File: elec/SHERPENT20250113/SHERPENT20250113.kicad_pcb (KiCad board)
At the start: 4 copper layers, 130.2 x 68.2 mm, 125 parts, among them J1 2137160001, J2 Conn_01x03_Socket, J3 Conn_01x03_Socket, Q1 NMOS, Q2 PMOS, Q3 NMOS, Q4 PMOS, SW1 CT1102, SW2 SW_Push, U1 MCP73831T-2ACI_OT, U2 TPS61288LRQQR, U4 TP4056, U5 LD1117S33TR_SOT223, U6 AN034_ANTENNA, U7 ESP32-C3, Y1 40MHz

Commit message: DRC ok
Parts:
- moved TP4 0.68 mm to (174.2, 86.2)
- moved R20 0.20 mm to (185.8, 83.2)
- moved R17 0.20 mm to (185.8, 79.8)
- moved R16 0.20 mm to (185.8, 81.5)
- moved C26 0.16 mm to (192.9, 77.0)
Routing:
- net GND: track 138.0 -> 139.8 mm
- net /VBATT: track 118.6 -> 117.8 mm
- net /VUSB: track 128.2 -> 129.0 mm
- net /StayOn: track 67.5 -> 68.2 mm
- net /Moteur2_PWM: track 62.6 -> 63.2 mm

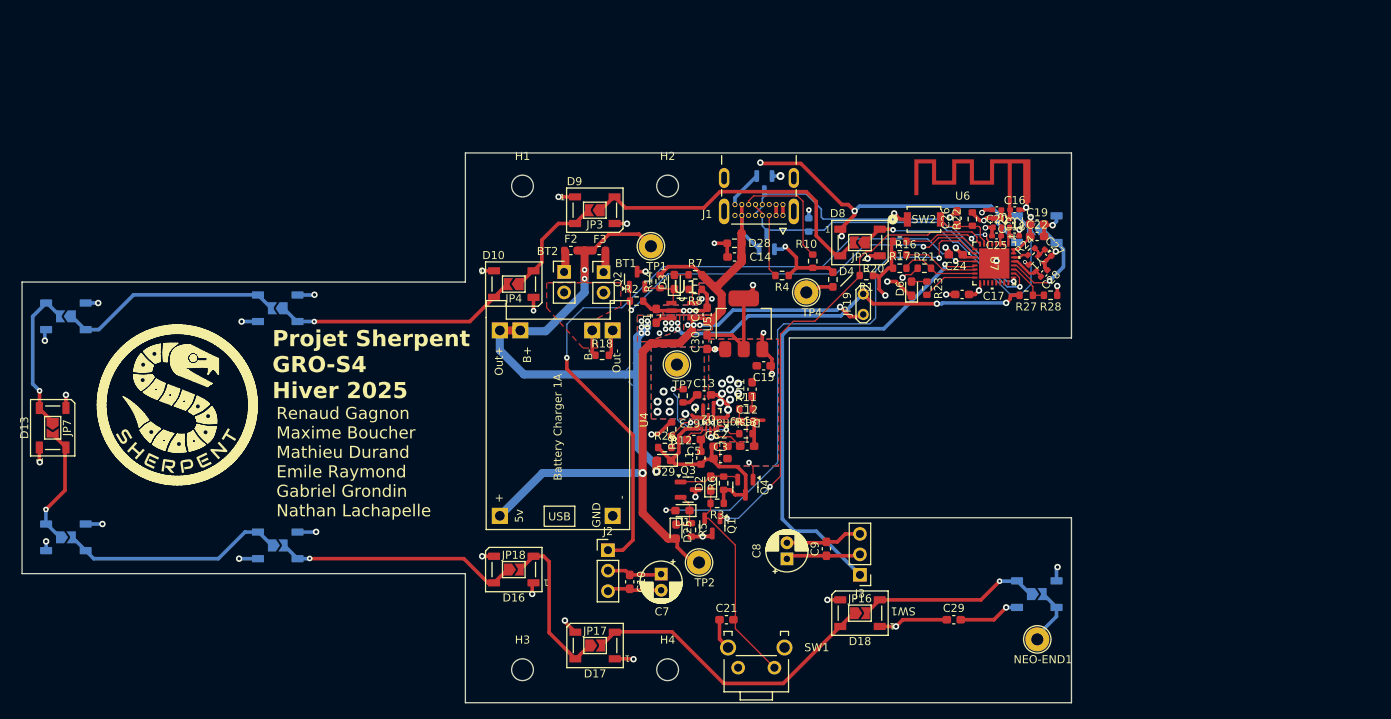
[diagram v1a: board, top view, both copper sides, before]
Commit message: Silkscreen done
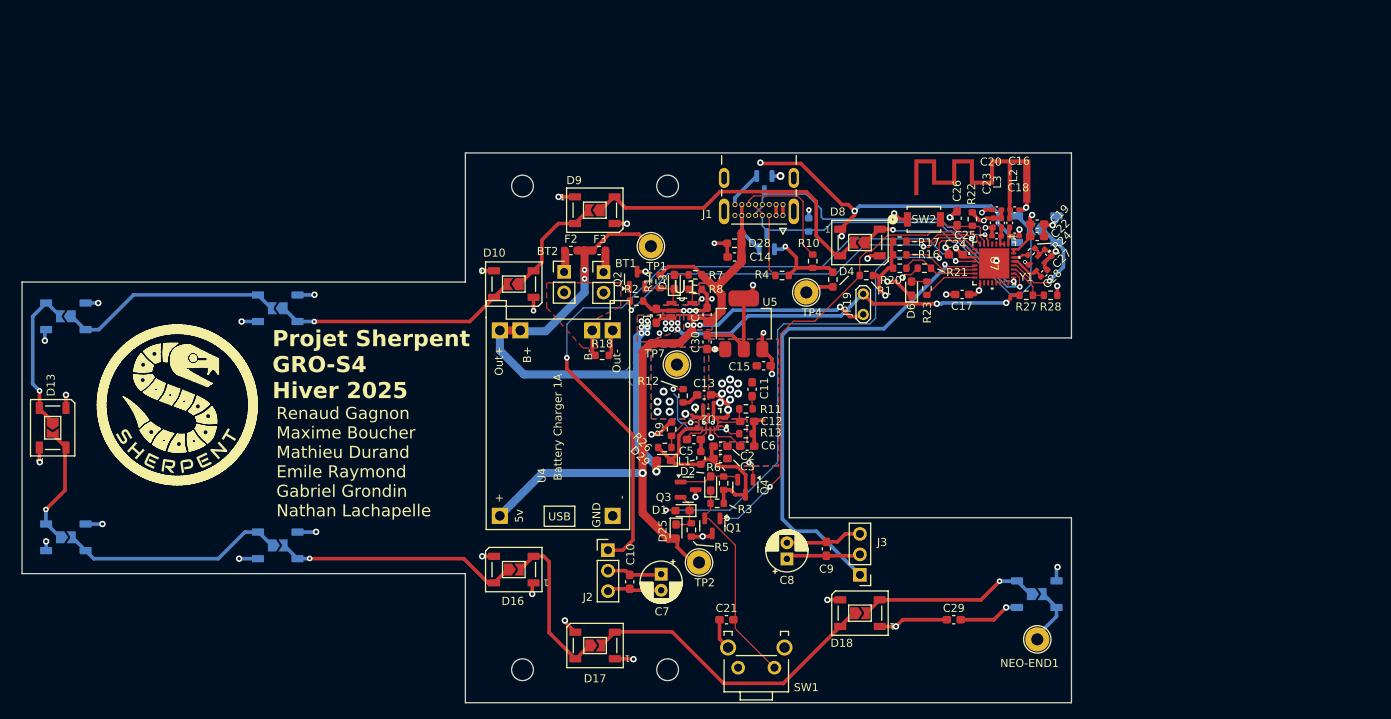
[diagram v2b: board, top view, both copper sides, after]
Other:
- board text removed: "J3"
- board text removed: "SW1"

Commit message: Conn neopx
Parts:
- removed D13, D14, D15: WS2812B, LED_SMD:LED_WS2812B_PLCC4_5.0x5.0mm_P3.2mm
- removed JP7, JP8, JP9: SolderJumper_2_Open, Jumper:SolderJumper-2_P1.3mm_Open_TrianglePad1.0x1.5mm
- added J4: Conn_01x03_Socket, Connector_PinHeader_2.54mm:PinHeader_1x03_P2.54mm_Vertical, F.Cu at (194.9, 133.2)
- moved JP6 65.6 mm to (137.9, 124.0), turned to 0 degrees
- moved D12 65.5 mm to (137.9, 123.9), turned to 180 degrees
- moved D11 30.1 mm to (138.1, 81.8)
- moved JP5 30.1 mm to (138.0, 81.8)
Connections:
- net Net-(D19-DOUT) renamed /neo_end
- D12 pad 2: Net-(D12-DOUT) -> /NEO_Row2
- JP6 pad 2: Net-(D12-DOUT) -> /NEO_Row2
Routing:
- net Net-(D14-DOUT): track 28.0 -> 0.00 mm
- net Net-(D11-DOUT): track 28.0 -> 48.8 mm
- net Net-(D10-DOUT): track 30.4 -> 9.92 mm
- net Net-(D12-DOUT): track 18.7 -> 0.00 mm, vias 1 -> 0
- net /NEO_Row2: track 30.5 -> 12.7 mm
- net Net-(D13-DOUT): track 15.3 -> 0.00 mm, vias 1 -> 0
- net +9V: track 111.0 -> 102.8 mm, vias 23 -> 18
- net /neo_end: track 7.36 -> 14.6 mm
- net GND: track 139.8 -> 133.8 mm, vias 48 -> 45
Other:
- board size 130.2 x 68.2 mm -> 75.2 x 68.2 mm
- board text added: "+ D G"
- board text added: "neopx"

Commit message: Gerber générés et PCB envoyé pour la fabrication
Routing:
- net +9V: track 102.8 -> 104.4 mm
- net Net-(U2-FB): track 14.0 -> 14.6 mm

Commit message: pcb V2 commencé
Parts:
- removed C1, C4: 4.7u, Capacitor_SMD:C_0603_1608Metric_Pad1.08x0.95mm_HandSolder
- removed C14, C24: 100n, Capacitor_SMD:C_0603_1608Metric_Pad1.08x0.95mm_HandSolder
- removed C18: 1.8p, Capacitor_SMD:C_0402_1005Metric_Pad0.74x0.62mm_HandSolder
- removed C19: 10n, Capacitor_SMD:C_0603_1608Metric_Pad1.08x0.95mm_HandSolder
- removed C20: 10u, Capacitor_SMD:C_0402_1005Metric_Pad0.74x0.62mm_HandSolder
- removed C22: 1u, Capacitor_SMD:C_0603_1608Metric_Pad1.08x0.95mm_HandSolder
- removed C23: 100n, Capacitor_SMD:C_0402_1005Metric_Pad0.74x0.62mm_HandSolder
- removed C25: 1u, Capacitor_SMD:C_0402_1005Metric_Pad0.74x0.62mm_HandSolder
- removed C27, C28: 15p, Capacitor_SMD:C_0402_1005Metric_Pad0.74x0.62mm_HandSolder
- removed D25: D_Schottky, LED_SMD:LED_0603_1608Metric_Pad1.05x0.95mm_HandSolder
- removed D29: D, Diode_SMD:D_0603_1608Metric_Pad1.05x0.95mm_HandSolder
- removed D3: LED, LED_SMD:LED_0603_1608Metric_Pad1.05x0.95mm_HandSolder
- removed D4: D_Zener, Resistor_SMD:R_0603_1608Metric_Pad0.98x0.95mm_HandSolder
- removed JP19: Jumper_2_Bridged, TestPoint:TestPoint_2Pads_Pitch2.54mm_Drill0.8mm
- removed L2: 2.7n, Inductor_SMD:L_0402_1005Metric_Pad0.77x0.64mm_HandSolder
- removed L3: 2n, Inductor_SMD:L_0402_1005Metric_Pad0.77x0.64mm_HandSolder
- removed Q4: PMOS, Package_TO_SOT_SMD:SOT-23
- removed R17, R20, R25: 10k, Resistor_SMD:R_0603_1608Metric
- removed R18, R21, R26: 0, Resistor_SMD:R_0603_1608Metric
- removed R24: 0, Resistor_SMD:R_0402_1005Metric_Pad0.72x0.64mm_HandSolder
- removed TP1: VBATT, TestPoint:TestPoint_Loop_D2.54mm_Drill1.5mm_Beaded
- removed U1: MCP73831T-2ACI_OT, MCP73831T_2ACI_OT:SOT95P280X145-5N
- removed U6: AN034_ANTENNA, AN034_ANTENNA:AN034_ANTENNA
- removed U7: ESP32-C3, ESP32_C3:QFN32_5X5_EXP-L
- removed Y1: 40MHz, 830059627:SMD_059627_WRE-L
- added C31: 47u, Capacitor_SMD:C_0603_1608Metric_Pad1.08x0.95mm_HandSolder, F.Cu at (161.8, 94.8)
- added C32: 47u, Capacitor_SMD:C_0603_1608Metric_Pad1.08x0.95mm_HandSolder, F.Cu at (161.8, 96.2)
- added C33: 47u, Capacitor_SMD:C_0603_1608Metric_Pad1.08x0.95mm_HandSolder, F.Cu at (161.8, 97.8)
- added JP7: BOOT, Connector_PinHeader_2.54mm:PinHeader_1x02_P2.54mm_Vertical, F.Cu at (178.8, 86.0)
- added Q5: PMOS, Package_TO_SOT_SMD:SOT-223, F.Cu at (186.2, 99.5)
- added R15: 10k, Resistor_SMD:R_0603_1608Metric, F.Cu at (242.9, 99.4)
- added R19: 10k, Resistor_SMD:R_0603_1608Metric, F.Cu at (242.9, 101.9)
- added SW3: BOOT, CS1213AGF160:SW_CS1213AG_CRS, F.Cu at (183.5, 86.8)
- added U3: LM66200DRLR, LM66200DRLR:SOT-5X3_DRL_TEX-L, F.Cu at (170.0, 88.2)
- added U8: ESP32-C3-WROOM-02, RF_Module:ESP32-C3-WROOM-02, F.Cu at (196.5, 82.2)
- C16: value 1.8p -> 10u; footprint Capacitor_SMD:C_0402_1005Metric_Pad0.74x0.62mm_HandSolder -> Capacitor_SMD:C_0603_1608Metric_Pad1.08x0.95mm_HandSolder
- C17: value 100n -> 0.1u
- C26: value 10n -> 0.1u
- H1, H2, H3, H4: footprint MountingHole:MountingHole_2.7mm_M2.5 -> MountingHole:MountingHole_3.2mm_M3
- L1: footprint Inductor_SMD:L_0603_1608Metric -> Inductor_SMD:L_1206_3216Metric
- NEO-END1: value TestPoint -> Neo-end
- Q1: value NMOS -> PMOS; footprint Package_TO_SOT_SMD:SOT-23 -> Package_TO_SOT_SMD:SOT-223
- Q2: value PMOS -> Q_NMOS_GSD
- Q3: value NMOS -> Q_NMOS_GSD
- R14, R2: value 100k -> 0; footprint Resistor_SMD:R_0603_1608Metric -> Resistor_SMD:R_1206_3216Metric
- R7: value 470 -> 0
- R8: value 2k -> 0; footprint Resistor_SMD:R_0603_1608Metric -> Resistor_SMD:R_1206_3216Metric
- SW2: value SW_Push -> RESET
- moved Q2 49.0 mm to (196.5, 107.5)
- moved TP2 41.3 mm to (158.5, 78.5)
- moved R2 34.0 mm to (174.5, 113.8)
- moved Q1 23.9 mm to (185.5, 108.5)
- moved R1 22.8 mm to (194.8, 102.8)
- moved R7 20.8 mm to (156.8, 104.5)
- moved C17 20.7 mm to (187.9, 66.5)
- moved R23 20.7 mm to (183.5, 65.8)
- moved R27 20.7 mm to (195.8, 66.6)
- moved R28 20.7 mm to (198.8, 66.6)
- moved R22 20.7 mm to (189.1, 57.2)
- moved C16 20.7 mm to (194.4, 56.0)
- moved C26 20.7 mm to (187.2, 57.1)
- moved D6 20.7 mm to (181.6, 65.8)
- moved TP7 18.8 mm to (177.0, 95.3)
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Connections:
- C15 pad 1: +9V -> /VDIODE
- C16 pad 1: Net-(U6-FP) -> +3.3V
- C2 pad 1: Net-(D29-K) -> Net-(U2-VIN)
- C29 pad 1: +9V -> +3.3V
- C3 pad 1: Net-(D29-K) -> Net-(U2-VIN)
- D10 pad 1: +9V -> +3.3V
- D11 pad 1: +9V -> +3.3V
- D12 pad 1: +9V -> +3.3V
- D16 pad 1: +9V -> +3.3V
- D17 pad 1: +9V -> +3.3V
- D18 pad 1: +9V -> +3.3V
- D19 pad 1: +9V -> +3.3V
- D7 pad 1: +9V -> +3.3V
- D8 pad 1: +9V -> +3.3V
- D9 pad 1: +9V -> +3.3V
- F2 pad 2: /VBATT -> Net-(Q5-S)
- F3 pad 2: /VBATT -> Net-(Q5-S)
- L1 pad 1: Net-(D29-K) -> Net-(U2-VIN)
- Q1 pad 1: /Button -> Net-(D2-A)
- Q1 pad 2: Net-(D2-K) -> Net-(U2-VIN)
- Q1 pad 3: GND -> /VBATT
- Q2 pad 1: /CHARGE -> Net-(D2-K)
- Q2 pad 2: Net-(D3-K) -> GND
- Q2 pad 3: +3.3V -> /Button
- Q3 pad 1: Net-(D2-A) -> Net-(D1-K)
- Q3 pad 2: Net-(D1-K) -> GND
- Q3 pad 3: GND -> Net-(D2-A)
- R14 pad 1: Net-(D3-K) -> Net-(Q5-S)
- R14 pad 2: /VUSB -> /VBATT
- R2 pad 1: GND -> /VBATT
- R2 pad 2: /CHARGE -> Net-(U2-VIN)
- R3 pad 1: Net-(D29-K) -> /VBATT
- R6 pad 1: Net-(D29-K) -> /VBATT
- R7 pad 1: Net-(D3-A) -> /VBATT
- R7 pad 2: /VUSB -> /BOOST_EN
- R8 pad 1: GND -> /B-
- R8 pad 2: Net-(U1-PROG) -> GND
- R9 pad 1: Net-(Q4-D) -> /BOOST_EN
- TP7 pad 1: +9V -> /VDIODE
- U2 pad 6: Net-(Q4-D) -> /BOOST_EN
- U2 pad 7: Net-(D29-K) -> Net-(U2-VIN)
- U5 pad 3: +9V -> /VDIODE
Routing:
- net /VUSB: track 129.0 -> 42.0 mm, vias 6 -> 2
- net /CHARGE: track 50.1 -> 0.00 mm, vias 2 -> 0
- net /VBATT: track 117.7 -> 69.8 mm, vias 18 -> 3
- net Net-(JP7-B): track 0.00 -> 43.6 mm
- net GND: track 133.8 -> 91.1 mm, vias 45 -> 20
- net /Moteur1_PWM: track 89.8 -> 57.9 mm, vias 2 -> 0
- net Net-(D2-K): track 26.2 -> 56.9 mm
- net /Button: track 59.5 -> 31.3 mm
- net Net-(D29-K): track 27.7 -> 0.00 mm
- net +3.3V: track 44.4 -> 20.0 mm, vias 8 -> 4
- net Net-(Q4-D): track 17.2 -> 0.00 mm, vias 2 -> 0
- net Net-(U2-VIN): track 0.00 -> 15.6 mm
- net /BOOST_EN: track 0.00 -> 14.8 mm, vias 0 -> 2
- net Net-(U7-GPIO2): track 12.0 -> 0.00 mm, vias 2 -> 0
- net Net-(U7-GPIO9): track 9.79 -> 0.00 mm
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- removed copper zone on F.Cu, net /VBATT
- removed copper zone on B.Cu, net /VUSB
- removed copper zone on F.Cu, net /VUSB

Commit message: Avancer PCB
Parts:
- removed R7: 0, Resistor_SMD:R_0603_1608Metric
- added Q6: PMOS, Package_TO_SOT_SMD:SOT-223, F.Cu at (220.0, 58.0)
- added R17: 0, Resistor_SMD:R_0603_1608Metric, F.Cu at (206.7, 98.0)
- added R18: 0, Resistor_SMD:R_1206_3216Metric, F.Cu at (217.9, 63.8)
- C13, C31, C32, C33, D8, JP2, U8: moved to B.Cu
- D7, JP1: moved to F.Cu
- L1: footprint Inductor_SMD:L_1206_3216Metric -> CMLE105T-2R2MS:IND_CMLE105T-1R0&slash_1R5&slash_2R2_CYN
- moved Q5 36.4 mm to (152.7, 85.1), turned to 90 degrees
- moved TP2 18.3 mm to (176.2, 73.8)
- moved L1 16.9 mm to (161.8, 111.0)
- moved R2 16.9 mm to (158.8, 120.0)
- moved R8 14.4 mm to (149.1, 94.7), turned to 0 degrees
- moved BT1 10.6 mm to (159.6, 82.9)
- moved F3 10.3 mm to (158.8, 80.0)
- moved R14 8.31 mm to (154.7, 90.7), turned to 180 degrees
- moved D7 6.71 mm to (196.1, 77.9)
- moved JP1 6.71 mm to (196.1, 77.9)
- moved C31 6.02 mm to (161.8, 100.8)
- moved SW2 5.47 mm to (187.9, 80.0)
- moved SW3 4.63 mm to (187.9, 88.2)
- moved C32 3.02 mm to (161.8, 99.3)
- moved D18 3.00 mm to (180.9, 129.0)
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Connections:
- F3 pad 2: Net-(Q5-S) -> Net-(Q6-S)
- R9 pad 1: /BOOST_EN -> /VBATT
- R9 pad 2: GND -> Net-(U2-EN)
- U2 pad 6: /BOOST_EN -> Net-(U2-EN)
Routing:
- net +9V: track 99.3 -> 16.7 mm, vias 16 -> 0
- net GND: track 91.1 -> 9.39 mm, vias 20 -> 0
- net /VBATT: track 69.8 -> 0.00 mm, vias 3 -> 0
- net /StayOn: track 60.0 -> 0.00 mm
- net /Moteur2_PWM: track 59.3 -> 0.00 mm
- net /Moteur1_PWM: track 57.9 -> 0.00 mm
- net Net-(D2-K): track 56.9 -> 0.00 mm
- net Net-(D11-DOUT): track 49.0 -> 0.00 mm
- net Net-(JP7-B): track 43.6 -> 0.00 mm
- net Net-(D8-DOUT): track 40.0 -> 0.00 mm
- net /USB_ESP32N: track 38.9 -> 0.00 mm
- net /USB_ESP32P: track 38.9 -> 0.00 mm
- net Net-(D17-DOUT): track 38.4 -> 0.00 mm
- net /VUSB: track 42.0 -> 8.52 mm, vias 2 -> 0
- net /Button: track 31.3 -> 0.00 mm, vias 2 -> 0
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- removed copper zone on B.Cu, net +9V
- removed copper zone on F.Cu, net +9V
- removed copper zone on F.Cu, net /B-
- removed copper zone on B.Cu, net /VBATT
- removed copper zone on B.Cu, net GND
- removed copper zone on F.Cu, net GND

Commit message: routing done. Good night.
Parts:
- removed C29: 1u, Capacitor_SMD:C_0603_1608Metric_Pad1.08x0.95mm_HandSolder
- removed D26, D27: BAV99, Package_TO_SOT_SMD:SOT-23
- removed NEO-END1: Neo-end, TestPoint:TestPoint_Loop_D2.54mm_Drill1.5mm_Beaded
- removed R14: 0, Resistor_SMD:R_1206_3216Metric
- removed R15: 10k, Resistor_SMD:R_0603_1608Metric
- added R20: 10k, Resistor_SMD:R_0603_1608Metric, F.Cu at (189.8, 83.8)
- added R21: 10k, Resistor_SMD:R_0603_1608Metric, F.Cu at (189.8, 86.3)
- added U1: TPD2EUSB30, Package_TO_SOT_SMD:Texas_DRT-3, F.Cu at (169.3, 78.9)
- C13, C31, C32, C33: moved to F.Cu
- Q6, R18: moved to B.Cu
- TP2: value TestPoint -> VUSB
- TP4: value TestPoint -> 3v3
- TP7: value TestPoint -> V_D
- moved Q6 72.4 mm to (152.5, 84.2), turned to -90 degrees
- moved R18 66.8 mm to (152.6, 78.1), turned to 180 degrees
- moved R19 62.6 mm to (184.5, 79.6)
- moved R17 50.3 mm to (156.4, 99.4)
- moved Q2 30.0 mm to (171.2, 123.6), turned to 0 degrees
- moved Q1 29.9 mm to (160.4, 124.8)
- moved C16 28.1 mm to (201.4, 83.2), turned to 180 degrees
- moved R22 24.7 mm to (204.3, 76.7), turned to 180 degrees
- moved C26 24.0 mm to (201.1, 76.7), turned to 180 degrees
- moved R1 24.0 mm to (184.5, 81.1), turned to 0 degrees
- moved R23 21.7 mm to (185.3, 87.4)
- moved D6 21.7 mm to (183.4, 87.4)
- moved C17 20.4 mm to (201.4, 81.7)
- moved R28 18.1 mm to (184.9, 78.1), turned to 0 degrees
- moved R16 16.5 mm to (201.5, 85.0)
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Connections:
- C11 pad 2: GND -> AGND
- C12 pad 2: GND -> AGND
- C6 pad 2: GND -> AGND
- R13 pad 2: GND -> AGND
- R23 pad 2: Net-(U8-IO10) -> Net-(U8-IO21/TXD)
- U2 pad 10: GND -> AGND
- U3 pad 7: /VDIODE -> unconnected-(U3-VOUT-Pad7)
- U3 pad 8: Net-(U3-ST) -> unconnected-(U3-ST-Pad8)
- U8 pad 10: Net-(U8-IO10) -> /BOOST_EN
- U8 pad 3: /BOOST_EN -> Net-(U8-IO4)
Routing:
- net +3.3V: track 0.00 -> 164.0 mm, vias 0 -> 14
- net /VBATT: track 0.00 -> 135.7 mm, vias 0 -> 4
- net GND: track 9.39 -> 112.0 mm, vias 0 -> 53
- net /VUSB: track 8.52 -> 96.8 mm, vias 0 -> 1
- net /Moteur1_PWM: track 0.00 -> 84.7 mm, vias 0 -> 1
- net /Moteur2_PWM: track 0.00 -> 78.0 mm
- net /StayOn: track 0.00 -> 74.8 mm, vias 0 -> 1
- net /Button: track 0.00 -> 55.1 mm, vias 0 -> 3
- net Net-(D11-DOUT): track 0.00 -> 48.5 mm
- net Net-(U2-VIN): track 0.00 -> 42.0 mm
- net /B-: track 0.00 -> 39.0 mm
- net Net-(D8-DOUT): track 0.00 -> 38.6 mm, vias 0 -> 3
- net Net-(D17-DOUT): track 0.00 -> 37.5 mm
- net Net-(JP7-B): track 0.00 -> 32.0 mm, vias 0 -> 1
- net /BOOST_EN: track 9.57 -> 38.2 mm, vias 0 -> 1
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- added copper zone on F.Cu, net +9V
- added copper zone on F.Cu, net GND

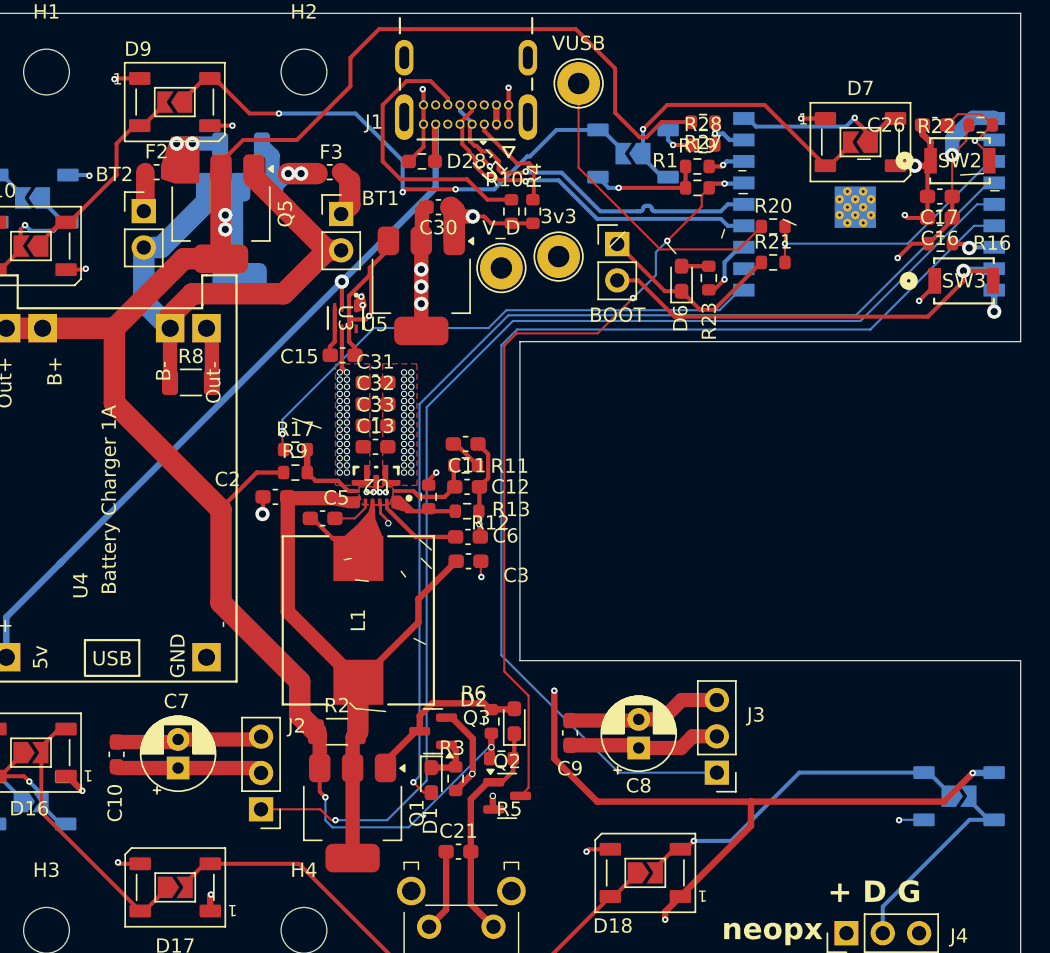
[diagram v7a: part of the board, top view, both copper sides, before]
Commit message: Reste le silkscreen
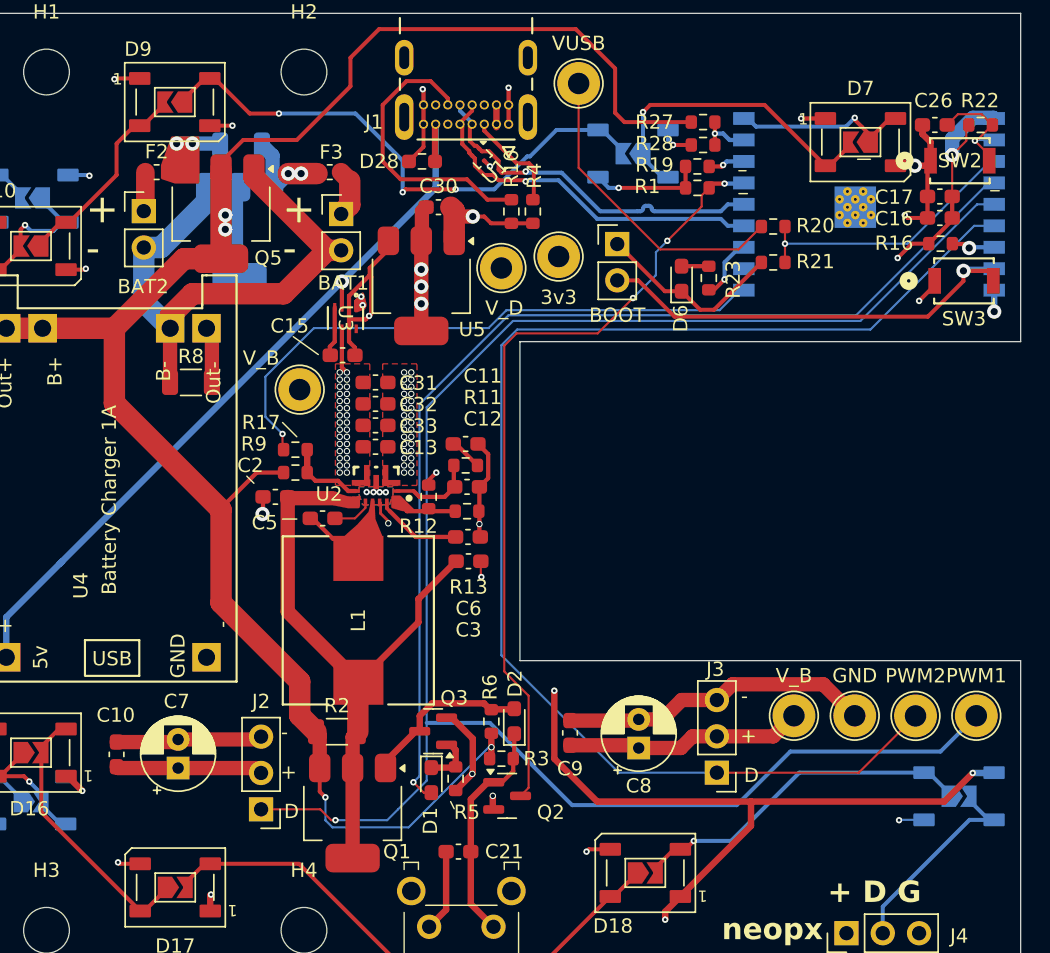
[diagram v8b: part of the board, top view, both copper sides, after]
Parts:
- added TP12: PWM1, TestPoint:TestPoint_Loop_D2.54mm_Drill1.5mm_Beaded, F.Cu at (204.0, 118.0)
- added TP13: PWM2, TestPoint:TestPoint_Loop_D2.54mm_Drill1.5mm_Beaded, F.Cu at (199.8, 118.0)
- added TP14: V_B, TestPoint:TestPoint_Loop_D2.54mm_Drill1.5mm_Beaded, F.Cu at (156.7, 95.2)
- added TP15: V_B, TestPoint:TestPoint_Loop_D2.54mm_Drill1.5mm_Beaded, F.Cu at (191.2, 118.0)
- added TP16: GND, TestPoint:TestPoint_Loop_D2.54mm_Drill1.5mm_Beaded, F.Cu at (195.5, 118.0)
- renumbered BT1 to BAT1, BT2 to BAT2
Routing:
- net /Moteur1_PWM: track 84.7 -> 128.1 mm
- net /Moteur2_PWM: track 78.0 -> 93.6 mm
- net GND: track 112.0 -> 123.0 mm
- net +9V: track 25.3 -> 31.2 mm
- net /BOOST_EN: track 38.2 -> 41.7 mm
- net /VBATT: track 135.7 -> 134.9 mm
- net Net-(D7-DOUT): track 22.1 -> 22.8 mm
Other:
- board text added: "+"
- board text added: "-"
- board text added: "D"
